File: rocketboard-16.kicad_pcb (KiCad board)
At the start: 2 copper layers, 86.2 x 99.9 mm, 103 parts, among them J1 OLED, J2 SWD, K1 KEYSW, K10 KEYSW, K11 KEYSW, K12 KEYSW, K13 KEYSW, K14 KEYSW, K15 KEYSW, K16 KEYSW, K2 KEYSW, K3 KEYSW, K4 KEYSW, K5 KEYSW, K6 KEYSW, K7 KEYSW, K8 KEYSW, K9 KEYSW, P1 USB_C_Plug_USB2.0, SW1 SW_Push, SW2 Rotary 1, SW3 Rotary 2, U1 STM32F103C8T6, U2 AMS1117-3.3, U3 USBLC6-2SC6, X1 8 MHz, Y1 32.768 kHz

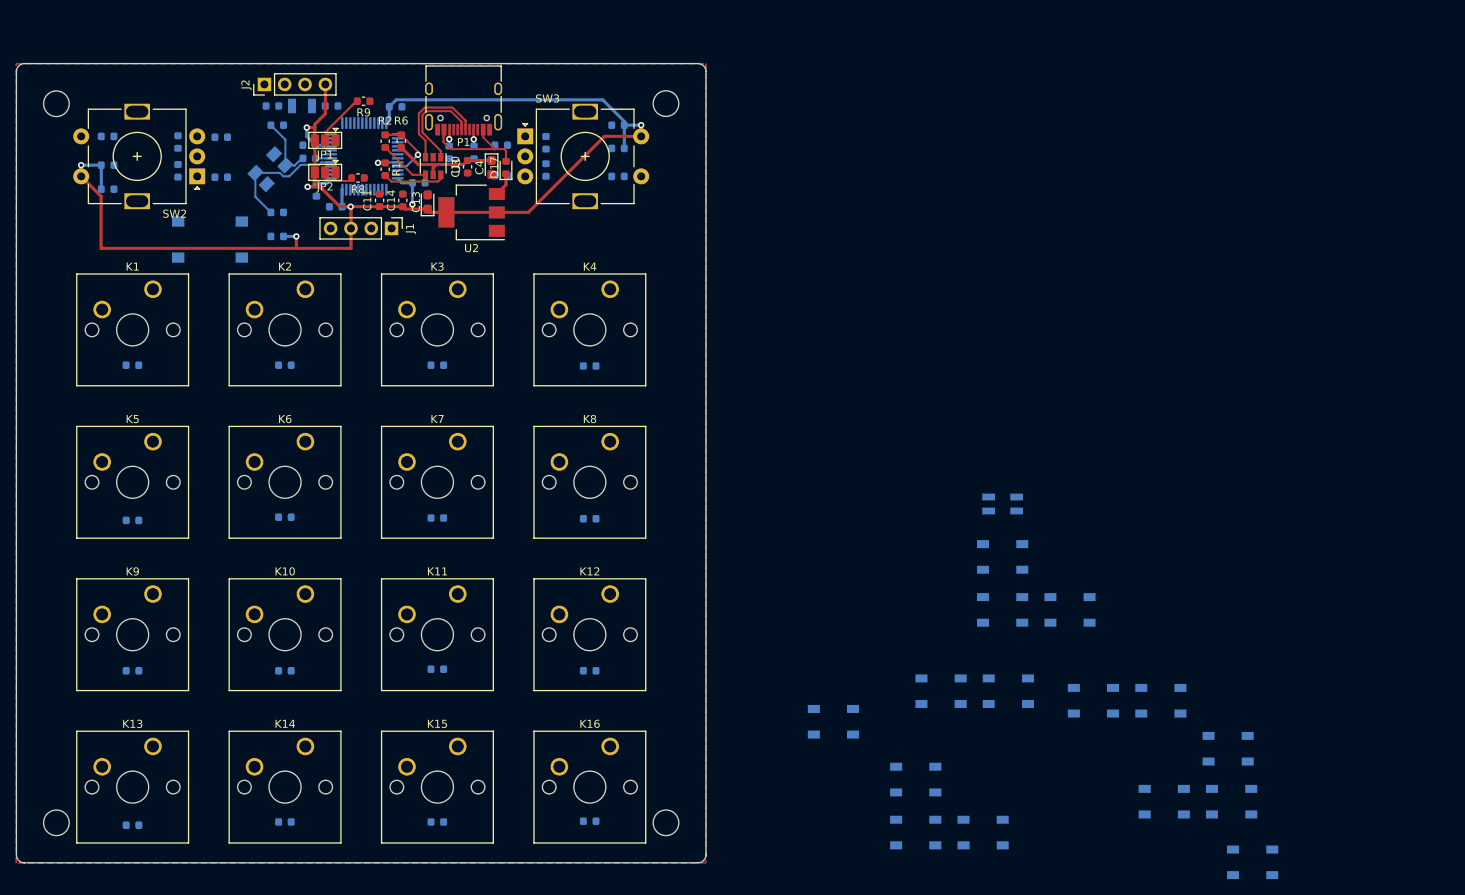
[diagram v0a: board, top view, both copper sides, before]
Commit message: Fixed the schematic issues (replaced keyswitch symbol for RGB LED, removed old LEDs, replaced USB-C connector), and moved those changes to PCBNew, but have not put all components onto board yet.
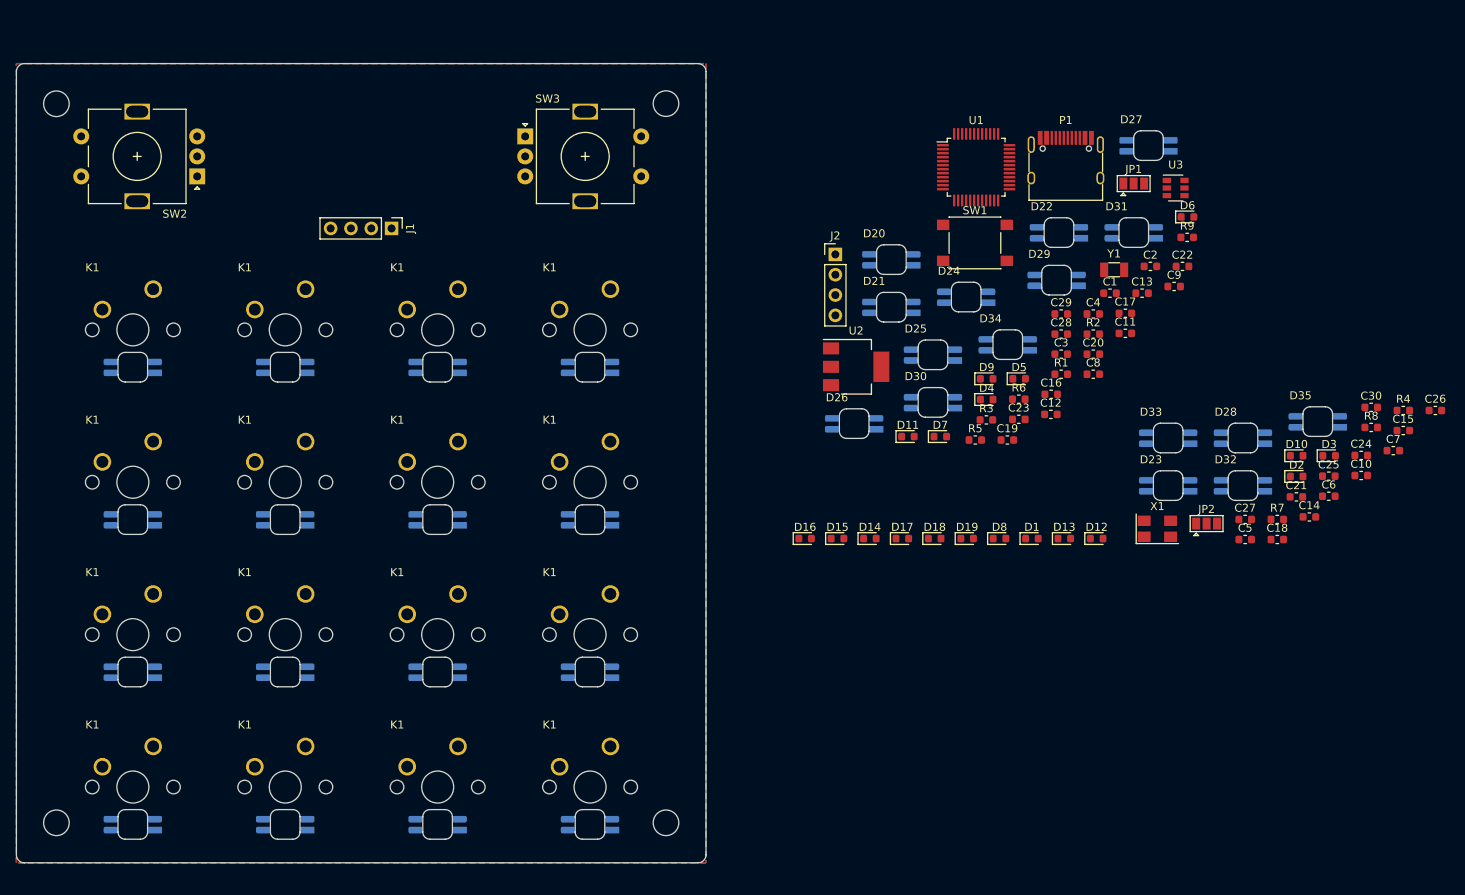
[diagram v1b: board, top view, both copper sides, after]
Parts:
- removed the K1 at (97.1, 79.6)
- removed K10, K11, K12, K13, K14, K15, K16, K2, K3, K4, K5, K6, K7, K8, K9: KEYSW, Button_Switch_Keyboard:SW_Cherry_MX_1.00u_PCB
- removed R10, R11, R12, R13, R14, R15, R16, R17, R18, R19: 10k, Resistor_SMD:R_0603_1608Metric
- added C19: 0.1u, Capacitor_SMD:C_0603_1608Metric, F.Cu at (203.9, 98.5)
- added C20: 0.1u, Capacitor_SMD:C_0603_1608Metric, F.Cu at (214.6, 87.7)
- added C21: 0.1u, Capacitor_SMD:C_0603_1608Metric, F.Cu at (240.0, 105.6)
- added C22: 0.1u, Capacitor_SMD:C_0603_1608Metric, F.Cu at (225.8, 76.8)
- added C23: 0.1u, Capacitor_SMD:C_0603_1608Metric, F.Cu at (205.3, 95.9)
- added C24: 0.1u, Capacitor_SMD:C_0603_1608Metric, F.Cu at (248.1, 100.4)
- added C25: 0.1u, Capacitor_SMD:C_0603_1608Metric, F.Cu at (244.1, 103.0)
- added C26: 0.1u, Capacitor_SMD:C_0603_1608Metric, F.Cu at (257.4, 94.8)
- added C27: 0.1u, Capacitor_SMD:C_0603_1608Metric, F.Cu at (233.6, 108.4)
- added C28: 0.1u, Capacitor_SMD:C_0603_1608Metric, F.Cu at (210.6, 85.2)
- added C29: 0.1u, Capacitor_SMD:C_0603_1608Metric, F.Cu at (210.6, 82.7)
- added C30: 0.1u, Capacitor_SMD:C_0603_1608Metric, F.Cu at (249.3, 94.4)
- added D34: SK6812MINI-E, josh-led:SK8612-MINI-E, F.Cu at (203.9, 86.6)
- added D35: SK6812MINI-E, josh-led:SK8612-MINI-E, F.Cu at (242.6, 96.2)
- added K1: MX_RGB, josh-keyboard:MX_KEYSWITCH_RGB, F.Cu at (151.7, 141.8)
- added K1: MX_RGB, josh-keyboard:MX_KEYSWITCH_RGB, F.Cu at (132.6, 103.8)
- added K1: MX_RGB, josh-keyboard:MX_KEYSWITCH_RGB, F.Cu at (113.5, 103.8)
- added K1: MX_RGB, josh-keyboard:MX_KEYSWITCH_RGB, F.Cu at (94.5, 103.8)
- added K1: MX_RGB, josh-keyboard:MX_KEYSWITCH_RGB, F.Cu at (151.7, 84.7)
- added K1: MX_RGB, josh-keyboard:MX_KEYSWITCH_RGB, F.Cu at (132.6, 84.7)
- added K1: MX_RGB, josh-keyboard:MX_KEYSWITCH_RGB, F.Cu at (113.5, 84.7)
- added K1: MX_RGB, josh-keyboard:MX_KEYSWITCH_RGB, F.Cu at (94.5, 84.7)
- added K1: MX_RGB, josh-keyboard:MX_KEYSWITCH_RGB, F.Cu at (132.6, 141.8)
- added K1: MX_RGB, josh-keyboard:MX_KEYSWITCH_RGB, F.Cu at (113.5, 141.8)
- added K1: MX_RGB, josh-keyboard:MX_KEYSWITCH_RGB, F.Cu at (94.5, 141.8)
- added K1: MX_RGB, josh-keyboard:MX_KEYSWITCH_RGB, F.Cu at (151.7, 122.8)
- added K1: MX_RGB, josh-keyboard:MX_KEYSWITCH_RGB, F.Cu at (132.6, 122.8)
- added K1: MX_RGB, josh-keyboard:MX_KEYSWITCH_RGB, F.Cu at (113.5, 122.8)
- added K1: MX_RGB, josh-keyboard:MX_KEYSWITCH_RGB, F.Cu at (94.5, 122.8)
- added K1: MX_RGB, josh-keyboard:MX_KEYSWITCH_RGB, F.Cu at (151.7, 103.8)
- C1, C12, C15, C16, C17, C18, C2, C3, C5, C6, C7, C8, C9, D1, D10, D11, D12, D13, D14, D15, D16, D2, D3, D4, D5, D6, D7, D8, D9, R3, R4, R5, R7, SW1, U1, X1, Y1: moved to F.Cu
- C13, C4: footprint Capacitor_Tantalum_SMD:CP_EIA-2012-12_Kemet-R -> Capacitor_SMD:C_0603_1608Metric
- D18, D19: value WS2812B -> D; footprint LED_SMD:LED_WS2812B_PLCC4_5.0x5.0mm_P3.2mm -> Diode_SMD:D_0603_1608Metric; moved to F.Cu
- D20, D21, D22, D23, D24, D25, D26, D27, D28, D30, D31, D32, D33: value WS2812B -> SK6812MINI-E; footprint LED_SMD:LED_WS2812B_PLCC4_5.0x5.0mm_P3.2mm -> josh-led:SK8612-MINI-E; moved to F.Cu
- D29: value LED_SK6812MINI_PLCC4_3.5x3.5mm_P1.75mm -> SK6812MINI-E; footprint LED_SMD:LED_SK6812MINI_PLCC4_3.5x3.5mm_P1.75mm -> josh-led:SK8612-MINI-E; moved to F.Cu
- P1: footprint Connector_USB:USB_C_Receptacle_HRO_TYPE-C-31-M-12 -> josh-connectors:USB_C_U262-161N-4BVC11
- moved C15 156.6 mm to (253.4, 97.3), turned to 0 degrees
- moved C6 134.8 mm to (244.1, 105.5), turned to 0 degrees
- moved R8 130.4 mm to (249.3, 96.9), turned to 0 degrees
- moved D10 129.3 mm to (240.0, 100.4), turned to 0 degrees
- moved R7 129.1 mm to (237.6, 108.4)
- moved D2 127.2 mm to (240.0, 103.0), turned to 0 degrees
- moved C7 126.3 mm to (252.1, 99.8)
- moved D13 121.9 mm to (211.0, 110.8), turned to 0 degrees
- moved R4 120.6 mm to (253.4, 94.8), turned to 0 degrees
- moved C14 120.0 mm to (241.6, 108.1), turned to 0 degrees
- moved X1 119.6 mm to (222.6, 109.5), turned to 0 degrees
- moved C5 119.2 mm to (233.6, 110.9)
- moved D6 118.9 mm to (226.4, 70.6), turned to 0 degrees
- moved JP2 118.6 mm to (228.8, 108.9), turned to 0 degrees
- moved C10 118.2 mm to (248.1, 102.9), turned to 0 degrees
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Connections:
- C15 pad 1: GND -> +5V
- C15 pad 2: Net-(C15-Pad2) -> GND
- C16 pad 1: Net-(C16-Pad1) -> +5V
- C17 pad 1: GND -> +5V
- C17 pad 2: Net-(C17-Pad2) -> GND
- C18 pad 1: Net-(C18-Pad1) -> +5V
- D1 pad 1: ROW0 -> ROW1
- D10 pad 1: ROW2 -> ROW3
- D11 pad 1: ROW2 -> ROW3
- D12 pad 1: ROW2 -> ROW3
- D13 pad 1: ROW3 -> Row4
- D14 pad 1: ROW3 -> Row4
- D15 pad 1: ROW3 -> Row4
- D16 pad 1: ROW3 -> Row4
- D18 pad 1: +5V -> ROW0
- D19 pad 1: +5V -> ROW0
- D2 pad 1: ROW0 -> ROW1
- D20 pad 1: +5V -> (no net)
- D20 pad 2: Net-(D20-Pad2) -> (no net)
- D20 pad 3: GND -> (no net)
- D20 pad 4: Net-(D19-Pad2) -> (no net)
- D21 pad 1: +5V -> (no net)
- D21 pad 2: Net-(D21-Pad2) -> (no net)
- D21 pad 3: GND -> (no net)
- D21 pad 4: Net-(D21-Pad4) -> (no net)
- D22 pad 1: +5V -> (no net)
- D22 pad 2: Net-(D22-Pad2) -> (no net)
- D22 pad 3: GND -> (no net)
- D22 pad 4: Net-(D18-Pad2) -> (no net)
- D23 pad 1: +5V -> (no net)
- D23 pad 2: Net-(D19-Pad4) -> (no net)
- D23 pad 3: GND -> (no net)
- D23 pad 4: Net-(D23-Pad4) -> (no net)
- D24 pad 1: +5V -> (no net)
- D24 pad 2: Net-(D24-Pad2) -> (no net)
- D24 pad 3: GND -> (no net)
- D24 pad 4: Net-(D20-Pad2) -> (no net)
- D25 pad 1: +5V -> (no net)
- D25 pad 2: Net-(D21-Pad4) -> (no net)
- D25 pad 3: GND -> (no net)
- D25 pad 4: Net-(D25-Pad4) -> (no net)
- D26 pad 1: +5V -> (no net)
- D26 pad 2: Net-(D26-Pad2) -> (no net)
- D26 pad 3: GND -> (no net)
- D26 pad 4: Net-(D22-Pad2) -> (no net)
- D27 pad 1: +5V -> (no net)
- D27 pad 2: Net-(D23-Pad4) -> (no net)
- D27 pad 3: GND -> (no net)
- D27 pad 4: Net-(D27-Pad4) -> (no net)
- D28 pad 1: +5V -> (no net)
- D28 pad 2: Net-(D28-Pad2) -> (no net)
- D28 pad 3: GND -> (no net)
- D28 pad 4: Net-(D24-Pad2) -> (no net)
- D29 pad 1: +5V -> (no net)
- D29 pad 2: Net-(D25-Pad4) -> (no net)
- D29 pad 3: GND -> (no net)
- D29 pad 4: Net-(D29-Pad4) -> (no net)
- D3 pad 1: ROW0 -> ROW1
- D30 pad 1: +5V -> (no net)
- D30 pad 2: Net-(D30-Pad2) -> (no net)
- D30 pad 3: GND -> (no net)
- D30 pad 4: Net-(D26-Pad2) -> (no net)
- D31 pad 1: +5V -> (no net)
- D31 pad 2: Net-(D27-Pad4) -> (no net)
- D31 pad 3: GND -> (no net)
- D31 pad 4: Net-(D30-Pad2) -> (no net)
- D32 pad 1: +5V -> (no net)
- D32 pad 2: Net-(D32-Pad2) -> (no net)
- D32 pad 3: GND -> (no net)
- D32 pad 4: Net-(D28-Pad2) -> (no net)
- D33 pad 1: +5V -> (no net)
- D33 pad 2: Net-(D29-Pad4) -> (no net)
- D33 pad 3: GND -> (no net)
- D33 pad 4: Net-(D32-Pad2) -> (no net)
- D4 pad 1: ROW0 -> ROW1
- D5 pad 1: ROW1 -> ROW2
- D6 pad 1: ROW1 -> ROW2
- D7 pad 1: ROW1 -> ROW2
- D8 pad 1: ROW1 -> ROW2
- D9 pad 1: ROW2 -> ROW3
- P1 pad A8: (no net) -> Net-(P1-PadA8)
- P1 pad B6: (no net) -> Net-(P1-PadA6)
- P1 pad B7: (no net) -> Net-(P1-PadA7)
- P1 pad B8: (no net) -> Net-(P1-PadB8)
- R5 pad 1: GND -> Net-(P1-PadB5)
- R5 pad 2: Net-(P1-PadB5) -> GND
- SW2 pad A: Net-(C15-Pad2) -> EC1_A
- SW2 pad B: Net-(C16-Pad1) -> EC1_B
- SW2 pad S1: EC1_S1 -> COL0
- SW2 pad S2: VCC -> Net-(D18-Pad2)
- SW3 pad A: Net-(C17-Pad2) -> EC2_A
- SW3 pad B: Net-(C18-Pad1) -> EC2_B
- SW3 pad S1: EC2_S1 -> COL3
- SW3 pad S2: VCC -> Net-(D19-Pad2)
- U1 pad 13: EC1_S1 -> Row4
- U1 pad 14: EC2_S1 -> Net-(U1-Pad14)
- X1 pad 2: GND -> Net-(C2-Pad1)
- X1 pad 3: Net-(C2-Pad1) -> GND
- X1 pad 4: GND -> (no net)
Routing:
- net VCC: track 173.7 -> 0.00 mm, vias 7 -> 0
- net +5V: track 17.1 -> 0.00 mm
- net OSC_IN: track 16.1 -> 0.00 mm
- net Net-(D17-Pad2): track 14.2 -> 0.00 mm
- net Net-(P1-PadA6): track 13.8 -> 0.00 mm
- net Net-(P1-PadA7): track 12.8 -> 0.00 mm
- net PA12: track 8.50 -> 0.00 mm, vias 1 -> 0
- net Net-(C2-Pad1): track 8.36 -> 0.00 mm
- net Net-(R1-Pad2): track 7.91 -> 0.00 mm
- net BOOT1: track 6.63 -> 0.00 mm
- net Net-(R2-Pad2): track 6.46 -> 0.00 mm
- net BOOT0: track 4.50 -> 0.00 mm
- net PA11: track 3.39 -> 0.00 mm, vias 1 -> 0
- net OSC_OUT: track 2.15 -> 0.00 mm
- net Net-(P1-PadB5): track 2.09 -> 0.00 mm, vias 1 -> 0
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
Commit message: Placed all componenets onto PCB and added josh's 3D model library in to get better 3D previews
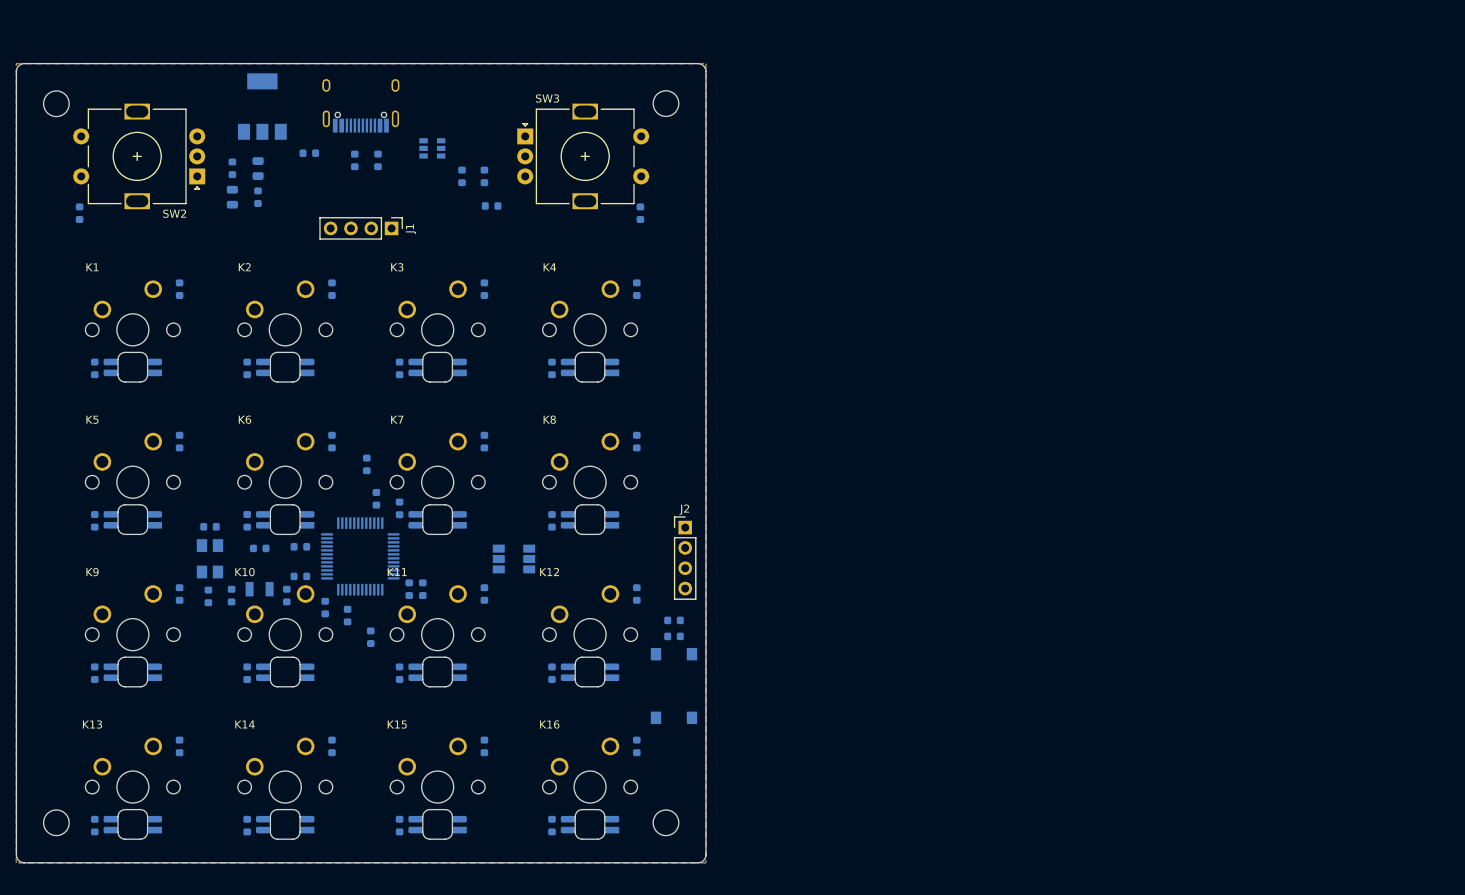
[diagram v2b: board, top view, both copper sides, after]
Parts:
- added C31: 1u, Capacitor_SMD:C_0603_1608Metric, B.Cu at (162.2, 121.0)
- C1, C11, C12, C14, C15, C16, C17, C18, C19, C2, C20, C21, C22, C23, C24, C25, C26, C27, C28, C29, C3, C30, C4, C5, C6, C7, C8, C9, D1, D10, D11, D12, D13, D14, D15, D16, D17, D18, D19, D2, D3, D4, D5, D6, D7, D8, D9, JP1, JP2, P1, R1, R2, R4, R5, R6, R7, R8, R9, SW1, U1, U2, U3, X1, Y1: moved to B.Cu
- C10, C13: footprint Capacitor_SMD:C_0603_1608Metric -> Capacitor_SMD:C_0805_2012Metric; moved to B.Cu
- D20, D21, D22, D23, D24, D25, D26, D27, D28, D29, D30, D31, D32, D33, D34, D35: footprint josh-led:SK8612-MINI-E -> josh-keyboard:DUMMY_SK6812MINI-E; moved to B.Cu
- R3: value 20 -> 10k; moved to B.Cu
- moved C15 163.7 mm to (89.8, 89.5), turned to 270 degrees
- moved C27 148.8 mm to (89.8, 146.7), turned to 270 degrees
- moved D32 145.1 mm to (94.5, 146.6)
- moved C10 143.1 mm to (110.2, 64.5), turned to 270 degrees
- moved C24 141.9 mm to (108.8, 127.6), turned to 270 degrees
- moved D28 141.8 mm to (94.5, 127.5)
- moved C14 137.4 mm to (110.2, 68.1), turned to 90 degrees
- moved C7 137.1 mm to (115.5, 111.8), turned to 180 degrees
- moved R4 134.7 mm to (122.3, 63.5), turned to 90 degrees
- moved C6 128.9 mm to (115.5, 115.5)
- moved R8 127.8 mm to (124.3, 123.1), turned to 270 degrees
- moved R7 127.2 mm to (110.4, 112.0)
- moved D10 122.9 mm to (118.6, 119.4), turned to 90 degrees
- moved D2 122.8 mm to (119.5, 79.6), turned to 90 degrees
- moved C2 122.0 mm to (104.2, 109.3), turned to 180 degrees
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- renumbered K1 to K10, K1 to K11, K1 to K12, K1 to K13, K1 to K14, K1 to K15, K1 to K16, K1 to K2, K1 to K3, K1 to K4, K1 to K5, K1 to K6, K1 to K7, K1 to K8, K1 to K9
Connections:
- K10 pad 1: Net-(D1-Pad2) -> Net-(D10-Pad2)
- K10 pad 2: COL0 -> COL1
- K10 pad 3: LED_SIG -> Net-(K10-Pad3)
- K10 pad 4: Net-(K1-Pad4) -> Net-(K10-Pad4)
- K11 pad 1: Net-(D1-Pad2) -> Net-(D11-Pad2)
- K11 pad 2: COL0 -> COL2
- K11 pad 3: LED_SIG -> Net-(K10-Pad4)
- K11 pad 4: Net-(K1-Pad4) -> Net-(K11-Pad4)
- K12 pad 1: Net-(D1-Pad2) -> Net-(D12-Pad2)
- K12 pad 2: COL0 -> COL3
- K12 pad 3: LED_SIG -> Net-(K11-Pad4)
- K12 pad 4: Net-(K1-Pad4) -> LED_R3
- K13 pad 1: Net-(D1-Pad2) -> Net-(D13-Pad2)
- K13 pad 3: LED_SIG -> LED_R3
- K13 pad 4: Net-(K1-Pad4) -> Net-(K13-Pad4)
- K14 pad 1: Net-(D1-Pad2) -> Net-(D14-Pad2)
- K14 pad 2: COL0 -> COL1
- K14 pad 3: LED_SIG -> Net-(K13-Pad4)
- K14 pad 4: Net-(K1-Pad4) -> Net-(K14-Pad4)
- K15 pad 1: Net-(D1-Pad2) -> Net-(D15-Pad2)
- K15 pad 2: COL0 -> COL2
- K15 pad 3: LED_SIG -> Net-(K14-Pad4)
- K15 pad 4: Net-(K1-Pad4) -> Net-(K15-Pad4)
- K16 pad 1: Net-(D1-Pad2) -> Net-(D16-Pad2)
- K16 pad 2: COL0 -> COL3
- K16 pad 3: LED_SIG -> Net-(K15-Pad4)
- K16 pad 4: Net-(K1-Pad4) -> Net-(K16-Pad4)
- K2 pad 1: Net-(D1-Pad2) -> Net-(D2-Pad2)
- K2 pad 2: COL0 -> COL1
- K2 pad 3: LED_SIG -> Net-(K1-Pad4)
- K2 pad 4: Net-(K1-Pad4) -> Net-(K2-Pad4)
- K3 pad 1: Net-(D1-Pad2) -> Net-(D3-Pad2)
- K3 pad 2: COL0 -> COL2
- K3 pad 3: LED_SIG -> Net-(K2-Pad4)
- K3 pad 4: Net-(K1-Pad4) -> Net-(K3-Pad4)
- K4 pad 1: Net-(D1-Pad2) -> Net-(D4-Pad2)
- K4 pad 2: COL0 -> COL3
- K4 pad 3: LED_SIG -> Net-(K3-Pad4)
- K4 pad 4: Net-(K1-Pad4) -> LED_R1
- K5 pad 1: Net-(D1-Pad2) -> Net-(D5-Pad2)
- K5 pad 3: LED_SIG -> LED_R1
- K5 pad 4: Net-(K1-Pad4) -> Net-(K5-Pad4)
- K6 pad 1: Net-(D1-Pad2) -> Net-(D6-Pad2)
- K6 pad 2: COL0 -> COL1
- K6 pad 3: LED_SIG -> Net-(K5-Pad4)
- K6 pad 4: Net-(K1-Pad4) -> Net-(K6-Pad4)
- K7 pad 1: Net-(D1-Pad2) -> Net-(D7-Pad2)
- K7 pad 2: COL0 -> COL2
- K7 pad 3: LED_SIG -> Net-(K6-Pad4)
- K7 pad 4: Net-(K1-Pad4) -> Net-(K7-Pad4)
- K8 pad 1: Net-(D1-Pad2) -> Net-(D8-Pad2)
- K8 pad 2: COL0 -> COL3
- K8 pad 3: LED_SIG -> Net-(K7-Pad4)
- K8 pad 4: Net-(K1-Pad4) -> LED_R2
- K9 pad 1: Net-(D1-Pad2) -> Net-(D9-Pad2)
- K9 pad 3: LED_SIG -> LED_R2
- K9 pad 4: Net-(K1-Pad4) -> Net-(K10-Pad3)
- X1 pad 2: Net-(C2-Pad1) -> GND
- X1 pad 3: GND -> Net-(C2-Pad1)
- X1 pad 4: (no net) -> GND

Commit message: Fixed some of the 3D model references, added a symbol/footprint for the SSD1306 OLED display with a 3D model for pictures, and added draft logo with board info
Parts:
- removed the J1 at (126.9, 72.0)
- added G***: LOGO, seth-logo:saturn_v_simplified, B.Cu at (84.1, 123.3)
- added REF**: Board Title, josh-logos:board-title, B.Cu at (84.6, 98.5)
- added U4: SSD1306_128x64, Connector_PinHeader_2.54mm:PinHeader_1x04_P2.54mm_Vertical, F.Cu at (126.9, 72.0)
- K1, K10, K11, K12, K13, K14, K15, K16, K2, K3, K4, K5, K6, K7, K8, K9: footprint josh-keyboard:MX_KEYSWITCH_RGB -> josh-keyboard:MX_KEYSWITCH_RGB_2D
- SW2, SW3: footprint Rotary_Encoder:RotaryEncoder_Alps_EC11E-Switch_Vertical_H20mm -> josh-buttons-switches:RotaryEncoder_Alps_EC11E-Switch_Vertical_H20mm_CircularMountingHoles
- renumbered J2 to J1
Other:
- board text removed: "SSD1306 OLED Display"
